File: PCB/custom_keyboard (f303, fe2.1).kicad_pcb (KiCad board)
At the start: 2 copper layers, 385.7 x 135.7 mm, 371 parts, among them IC1 FE2.1, J2 Conn_01x03_Male, Q1 DTC123J, SW1 SW_Push, U1 24LC02BT-I/SN, U10 PRTR5V0U2X, U11 XC6206P332MR, U12 74LVC1G34, U2 PRTR5V0U2X, U4 PRTR5V0U2X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

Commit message: Made tweaks to layout
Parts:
- J2: footprint Connector_JST:JST_GH_SM03B-GHS-TB_1x03-1MP_P1.25mm_Horizontal -> Connector_JST:JST_SH_SM03B-SRSS-TB_1x03-1MP_P1.00mm_Horizontal
- moved C36 14.0 mm to (474.6, 254.8), turned to 90 degrees
- moved U6 3.97 mm to (150.8, 204.8)
- moved R14 3.57 mm to (505.2, 191.3)
- moved R31 2.38 mm to (156.4, 206.0)
- moved R33 2.38 mm to (156.4, 203.6)
- moved F6 2.14 mm to (183.7, 188.9)
- moved R36 1.77 mm to (146.8, 206.4)
- moved J2 1.64 mm to (280.2, 292.9)
- moved C25 1.64 mm to (186.5, 188.9)
- moved F5 1.64 mm to (143.7, 211.1)
- moved F3 1.59 mm to (508.8, 198.4)
- moved R2 1.28 mm to (280.6, 196.8)
- moved R4 1.28 mm to (283.0, 196.8)
- moved C7 1.19 mm to (508.8, 192.5), turned to 90 degrees
- moved C8 1.19 mm to (508.8, 187.7), turned to 90 degrees
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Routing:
- net GND: track 789.7 -> 763.3 mm, vias 265 -> 291
- net +3V3: track 278.9 -> 295.0 mm
- net +5V: track 3527.1 -> 3538.1 mm, vias 12 -> 8
- net HUB_DRV: track 60.6 -> 66.7 mm
- net Earth: track 525.6 -> 519.8 mm, vias 33 -> 32
- net DOUT1: track 371.1 -> 376.4 mm
- net ENCODER_A: track 641.5 -> 637.9 mm
- net ENCODER_B2: track 290.9 -> 287.3 mm
- net EXTRA_1: track 55.0 -> 58.2 mm
- net Net-(C7-Pad2): track 8.66 -> 11.3 mm
- net Net-(R33-Pad1): track 15.5 -> 17.9 mm
- net Net-(R31-Pad1): track 14.3 -> 16.7 mm
- net HUB_PORT2_D-: track 357.5 -> 355.1 mm
- net HUB_PORT2_D+: track 357.3 -> 354.9 mm
- net ROT1_ROW: track 663.0 -> 665.0 mm
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
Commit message: Drew outlines for case
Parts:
- moved R2 114.1 mm to (390.9, 225.8)
- moved R4 114.1 mm to (393.3, 225.8)
- moved USB2 66.5 mm to (71.4, 182.6)
- moved R19 66.4 mm to (437.7, 185.3)
- moved R20 66.4 mm to (437.7, 182.9)
- moved C31 65.9 mm to (384.8, 230.2)
- moved R41 65.9 mm to (384.8, 227.8)
- moved U4 64.3 mm to (446.9, 182.6)
- moved R24 63.8 mm to (428.2, 175.4)
- moved R25 63.8 mm to (425.8, 175.4)
- moved C11 63.0 mm to (409.5, 228.6)
- moved C12 63.0 mm to (411.9, 228.6)
- moved C14 63.0 mm to (404.8, 232.6)
- moved C17 63.0 mm to (278.2, 279.0)
- moved C20 63.0 mm to (263.5, 265.1)
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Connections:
- R19 pad 1: Net-(R19-Pad1) -> D+
- R2 pad 1: Net-(R2-Pad1) -> D-
- R20 pad 1: Net-(R20-Pad1) -> D-
- R24 pad 1: Net-(R24-Pad1) -> D+
- R25 pad 1: Net-(R25-Pad1) -> D-
- R3 pad 2: Net-(R3-Pad2) -> D-
- R31 pad 1: Net-(R31-Pad1) -> D-
- R33 pad 1: Net-(R33-Pad1) -> D+
- R34 pad 1: Net-(R34-Pad1) -> D+
- R37 pad 1: Net-(R37-Pad1) -> D-
- R4 pad 1: Net-(R4-Pad1) -> D+
- R43 pad 1: Net-(R43-Pad1) -> KEYBOARD_D-
- R44 pad 1: Net-(R44-Pad1) -> KEYBOARD_D+
- R45 pad 1: Net-(R45-Pad1) -> D+
- R46 pad 1: Net-(R46-Pad1) -> D-
- R6 pad 2: Net-(R6-Pad2) -> D+
- U10 pad 2: Net-(R45-Pad1) -> D+
- U10 pad 3: Net-(R46-Pad1) -> D-
- U2 pad 2: Net-(R4-Pad1) -> D+
- U2 pad 3: Net-(R2-Pad1) -> D-
- U4 pad 2: Net-(R19-Pad1) -> D+
- U4 pad 3: Net-(R20-Pad1) -> D-
- U5 pad 2: Net-(R24-Pad1) -> D+
- U5 pad 3: Net-(R25-Pad1) -> D-
- U6 pad 2: Net-(R33-Pad1) -> D+
- U6 pad 3: Net-(R31-Pad1) -> D-
- U9 pad 32: Net-(R43-Pad1) -> KEYBOARD_D-
- U9 pad 33: Net-(R44-Pad1) -> KEYBOARD_D+
- USB1 pad 5: Net-(R2-Pad1) -> D-
- USB1 pad 6: Net-(R4-Pad1) -> D+
- USB1 pad 7: Net-(R2-Pad1) -> D-
- USB1 pad 8: Net-(R4-Pad1) -> D+
- USB2 pad 5: Net-(R31-Pad1) -> D-
- USB2 pad 6: Net-(R33-Pad1) -> D+
- USB2 pad 7: Net-(R31-Pad1) -> D-
- USB2 pad 8: Net-(R33-Pad1) -> D+
- USB3 pad 2: Net-(R37-Pad1) -> D-
- USB3 pad 3: Net-(R34-Pad1) -> D+
- USB4 pad 2: Net-(R46-Pad1) -> D-
- USB4 pad 3: Net-(R45-Pad1) -> D+
- USB5 pad 5: Net-(R3-Pad2) -> D-
- USB5 pad 6: Net-(R6-Pad2) -> D+
- USB5 pad 7: Net-(R3-Pad2) -> D-
- USB5 pad 8: Net-(R6-Pad2) -> D+
- USB6 pad 2: Net-(R25-Pad1) -> D-
- USB6 pad 3: Net-(R24-Pad1) -> D+
- USB7 pad 5: Net-(R20-Pad1) -> D-
- USB7 pad 6: Net-(R19-Pad1) -> D+
- USB7 pad 7: Net-(R20-Pad1) -> D-
- USB7 pad 8: Net-(R19-Pad1) -> D+
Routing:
- net D+: track 0.00 -> 338.3 mm
- net D-: track 0.00 -> 334.2 mm
- net HUB_D-: track 224.6 -> 5.62 mm
- net HUB_D+: track 224.6 -> 5.62 mm
- net Earth: track 519.8 -> 401.6 mm, vias 32 -> 31
- net Net-(R6-Pad2): track 21.1 -> 0.00 mm
- net Net-(R4-Pad1): track 21.1 -> 0.00 mm
- net Net-(R3-Pad2): track 19.8 -> 0.00 mm
- net Net-(R2-Pad1): track 19.7 -> 0.00 mm
- net Net-(R33-Pad1): track 17.9 -> 0.00 mm
- net Net-(R31-Pad1): track 16.7 -> 0.00 mm
- net Net-(R25-Pad1): track 14.7 -> 0.00 mm
- net Net-(R24-Pad1): track 14.7 -> 0.00 mm
- net Net-(R19-Pad1): track 14.6 -> 0.00 mm
- net Net-(R20-Pad1): track 13.4 -> 0.00 mm
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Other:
- board size 385.7 x 135.7 mm -> 388.1 x 135.7 mm

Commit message: Moved microcontroller and side USBs
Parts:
- added MX83: SPACE, custom-footprints:CherryMX_6.25u_PCB_KailhSocket_LTST-A683CEGBW, F.Cu at (234.1, 273.0)
- added MX84: RALT, custom-footprints:CherryMX_1.25u_PCB_KailhSocket_LTST-A683CEGBW, F.Cu at (305.6, 273.0)
- moved U8 14.4 mm to (278.6, 274.2)
- moved R36 5.56 mm to (81.8, 185.7), turned to 270 degrees
- moved R43 4.44 mm to (290.1, 273.0)
- moved R44 4.37 mm to (290.1, 275.4)
- moved C23 4.27 mm to (89.7, 185.7), turned to 0 degrees
- moved F5 4.05 mm to (84.9, 186.5), turned to 90 degrees
- moved C18 3.27 mm to (261.1, 282.6)
- moved C19 3.27 mm to (258.7, 282.6)
- moved R35 3.18 mm to (83.3, 180.1)
- moved C1 3.17 mm to (248.0, 271.0)
- moved C16 3.17 mm to (273.0, 267.9)
- moved C17 3.17 mm to (275.0, 279.0)
- moved C20 3.17 mm to (260.3, 265.1)
- moved C21 3.17 mm to (262.7, 265.1)
- moved C3 3.17 mm to (251.6, 266.7)
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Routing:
- net COL16: track 258.1 -> 362.4 mm
- net GND: track 755.2 -> 694.8 mm, vias 287 -> 291
- net Earth: track 401.6 -> 355.3 mm, vias 31 -> 30
- net COL6: track 180.2 -> 203.6 mm
- net +5V: track 3526.5 -> 3542.2 mm
- net COL14: track 256.1 -> 241.0 mm
- net COL2: track 323.1 -> 310.0 mm
- net +3V3: track 294.9 -> 287.9 mm
- net KEYBOARD_D+: track 176.9 -> 183.8 mm
- net ROW5: track 540.8 -> 546.7 mm, vias 4 -> 5
- net COL9: track 143.9 -> 149.0 mm
- net ENCODER_A: track 637.9 -> 642.4 mm
- net COL17: track 297.9 -> 302.4 mm
- net ENCODER_B1: track 636.8 -> 641.3 mm
- net ENCODER_B2: track 287.3 -> 291.7 mm
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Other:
- board size 388.1 x 135.7 mm -> 390.5 x 135.7 mm

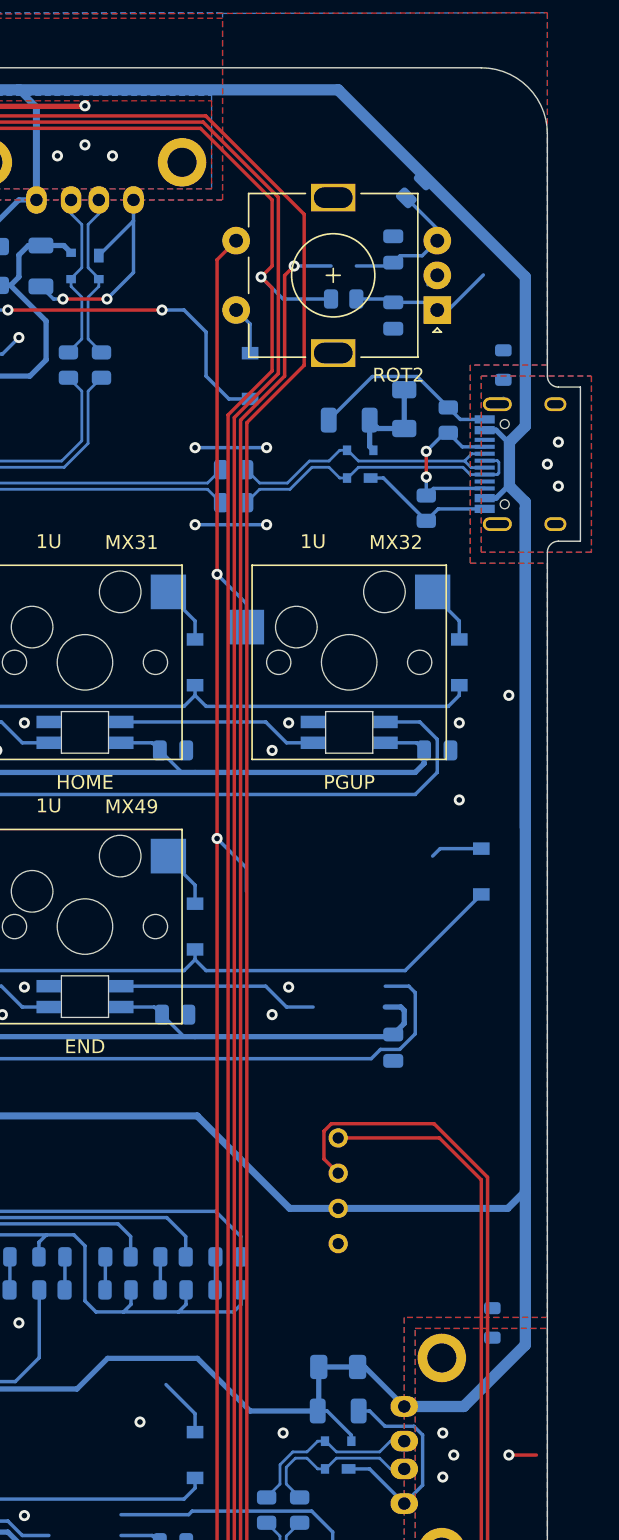
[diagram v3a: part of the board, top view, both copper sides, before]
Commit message: Connected earth
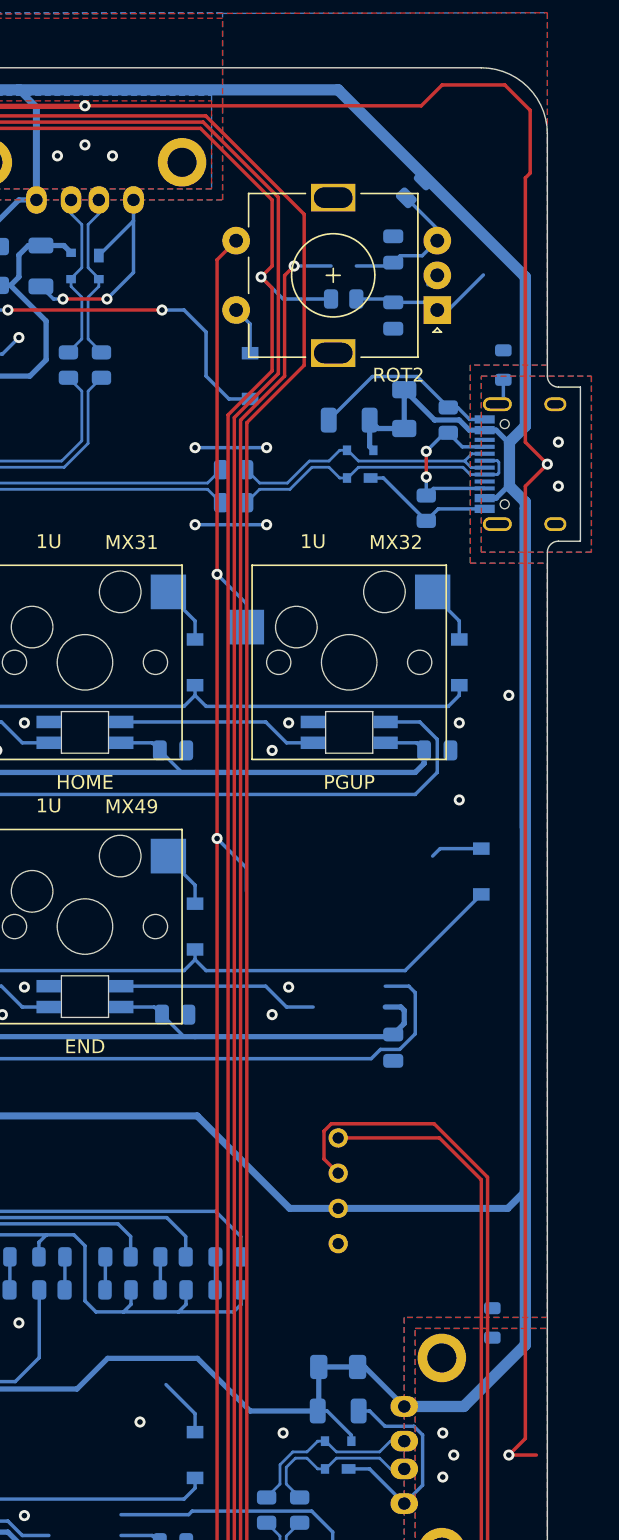
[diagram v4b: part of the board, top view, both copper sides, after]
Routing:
- net Earth: track 355.3 -> 489.0 mm
- net +5V: track 3542.2 -> 3549.2 mm
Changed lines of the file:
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@@
     (thickness 1.6)
     (drawings 57)
-    (tracks 3854)
+    (tracks 3871)
     (zones 0)
     (modules 422)
@@
   )
   (setup
-    (last_trace_width 0.8128)
+    (last_trace_width 0.25)
     (user_trace_width 0.2)
     (user_trace_width 0.254)
@@
   (segment (start 447.72811 176.23249) (end 450.97149 176.23249) (width 0.25) (layer B.Cu) (net 1))
   (segment (start 444.5844 179.3762) (end 447.72811 176.23249) (width 0.25) (layer B.Cu) (net 1) (status 10))
-  (segment (start 454.065 179.326) (end 453.2027 178.4637) (width 0.25) (layer B.Cu) (net 1) (status 20))
-  (segment (start 455.8258 179.326) (end 454.065 179.326) (width 0.25) (layer B.Cu) (net 1) (status 10))
   (segment (start 452.4776 185.776) (end 451.6153 186.6383) (width 0.25) (layer B.Cu) (net 1) (status 20))
   (segment (start 455.8258 185.776) (end 452.4776 185.776) (width 0.25) (layer B.Cu) (net 1) (status 10))
@@
   (via (at 452.80585 252.3966) (size 0.8) (drill 0.4) (layers F.Cu B.Cu) (net 12))
   (via (at 452.80585 255.5714) (size 0.8) (drill 0.4) (layers F.Cu B.Cu) (net 12))
-  (segment (start 457.1712 177.8006) (end 456.7408 178.231) (width 0.25) (layer B.Cu) (net 12) (status 30))
   (via (at 126.992 159.93055) (size 0.8) (drill 0.4) (layers F.Cu B.Cu) (net 12))
   (via (at 136.5164 159.93055) (size 0.8) (drill 0.4) (layers F.Cu B.Cu) (net 12))
@@
   (via (at 282.5572 260.3336) (size 0.8) (drill 0.4) (layers F.Cu B.Cu) (net 1))
   (via (at 256.3651 281.7635) (size 0.8) (drill 0.4) (layers F.Cu B.Cu) (net 1))
+  (segment (start 453.2027 178.4637) (end 453.8776 178.4637) (width 0.25) (layer B.Cu) (net 1))
+  (segment (start 454.7399 179.326) (end 455.8258 179.326) (width 0.25) (layer B.Cu) (net 1))
+  (segment (start 453.8776 178.4637) (end 454.7399 179.326) (width 0.25) (layer B.Cu) (net 1))
   (segment (start 291.9754 273.99835) (end 291.00985 273.0328) (width 0.2) (layer B.Cu) (net 129) (status 20))
   (segment (start 279.5387 273.22335) (end 279.4887 273.22335) (width 0.2) (layer B.Cu) (net 2) (status 30))
@@
   (segment (start 77.396589 184.095647) (end 76.1952 185.297036) (width 0.8128) (layer B.Cu) (net 2))
   (segment (start 76.1952 185.7258) (end 76.1952 199.2187) (width 0.8128) (layer B.Cu) (net 2))
+  (segment (start 452.21211 179.36671) (end 450.0279 177.1825) (width 0.381) (layer B.Cu) (net 2))
+  (segment (start 453.98551 179.36671) (end 452.21211 179.36671) (width 0.381) (layer B.Cu) (net 2))
+  (segment (start 454.7198 180.101) (end 453.98551 179.36671) (width 0.381) (layer B.Cu) (net 2))
+  (segment (start 455.8258 180.101) (end 454.7198 180.101) (width 0.381) (layer B.Cu) (net 2))
   (via (at 73.8141 184.1384) (size 0.8) (drill 0.4) (layers F.Cu B.Cu) (net 12))
   (via (at 73.8141 180.9636) (size 0.8) (drill 0.4) (layers F.Cu B.Cu) (net 12))
   (via (at 74.6078 182.551) (size 0.8) (drill 0.4) (layers F.Cu B.Cu) (net 12))
+  (segment (start 457.1712 177.8006) (end 456.7408 178.231) (width 0.25) (layer B.Cu) (net 12))
+  (segment (start 457.1712 176.4702) (end 457.1712 177.8006) (width 0.25) (layer B.Cu) (net 12))
+  (segment (start 427.0106 156.71813) (end 451.25607 156.71813) (width 0.25) (layer F.Cu) (net 12))
+  (segment (start 457.275801 155.214999) (end 459.108801 157.047999) (width 0.25) (layer F.Cu) (net 12))
+  (segment (start 452.759201 155.214999) (end 457.275801 155.214999) (width 0.25) (layer F.Cu) (net 12))
+  (segment (start 459.108801 157.047999) (end 459.108801 161.564599) (width 0.25) (layer F.Cu) (net 12))
+  (segment (start 451.25607 156.71813) (end 452.759201 155.214999) (width 0.25) (layer F.Cu) (net 12))
+  (segment (start 459.108801 161.564599) (end 458.7586 161.9148) (width 0.25) (layer F.Cu) (net 12))
+  (segment (start 458.7586 180.9636) (end 460.346 182.551) (width 0.25) (layer F.Cu) (net 12))
+  (segment (start 458.7586 161.9148) (end 458.7586 180.9636) (width 0.25) (layer F.Cu) (net 12))
+  (segment (start 460.346 182.551) (end 458.7586 184.1384) (width 0.25) (layer F.Cu) (net 12))
+  (segment (start 458.7586 252.79345) (end 457.56805 253.984) (width 0.25) (layer F.Cu) (net 12))
+  (segment (start 458.7586 184.1384) (end 458.7586 252.79345) (width 0.25) (layer F.Cu) (net 12))
   (via (at 292.8753 268.2706) (size 0.8) (drill 0.4) (layers F.Cu B.Cu) (net 29))
   (segment (start 292.528901 267.924201) (end 292.8753 268.2706) (width 0.25) (layer F.Cu) (net 29))
